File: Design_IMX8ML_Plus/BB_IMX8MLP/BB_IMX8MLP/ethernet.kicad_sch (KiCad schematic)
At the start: 40 parts, among them J5 RJ45_JK0654219, J6 RJ45_JK0654219, U1 KSZ9131RNXI, Y2 25MHz

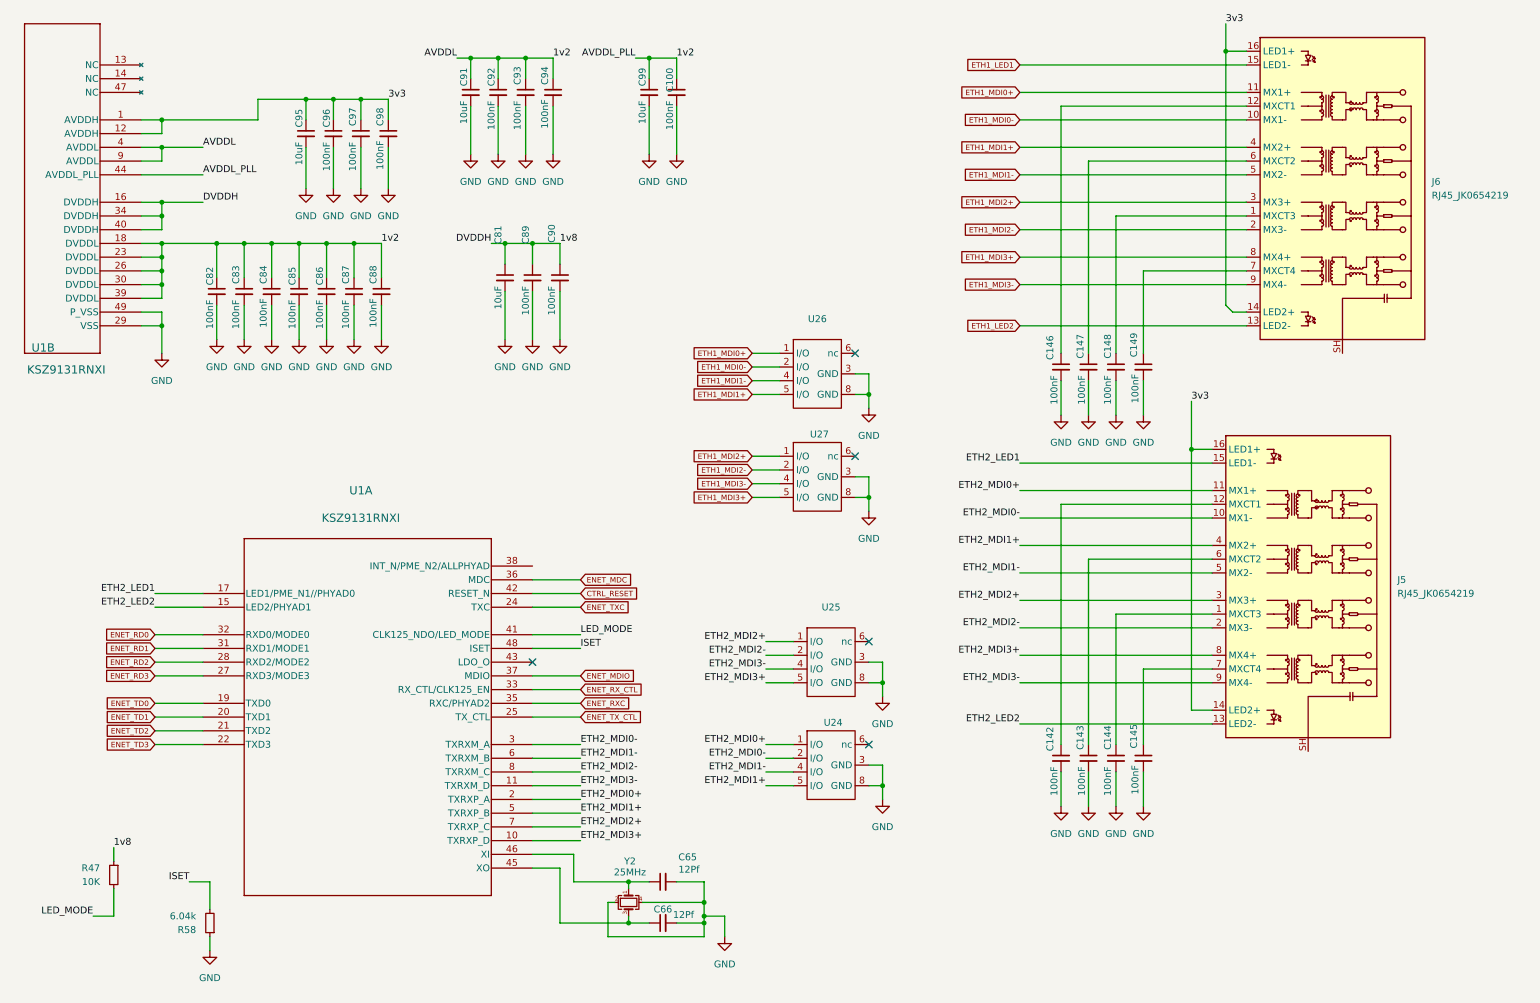
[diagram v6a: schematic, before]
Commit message: Board base resize
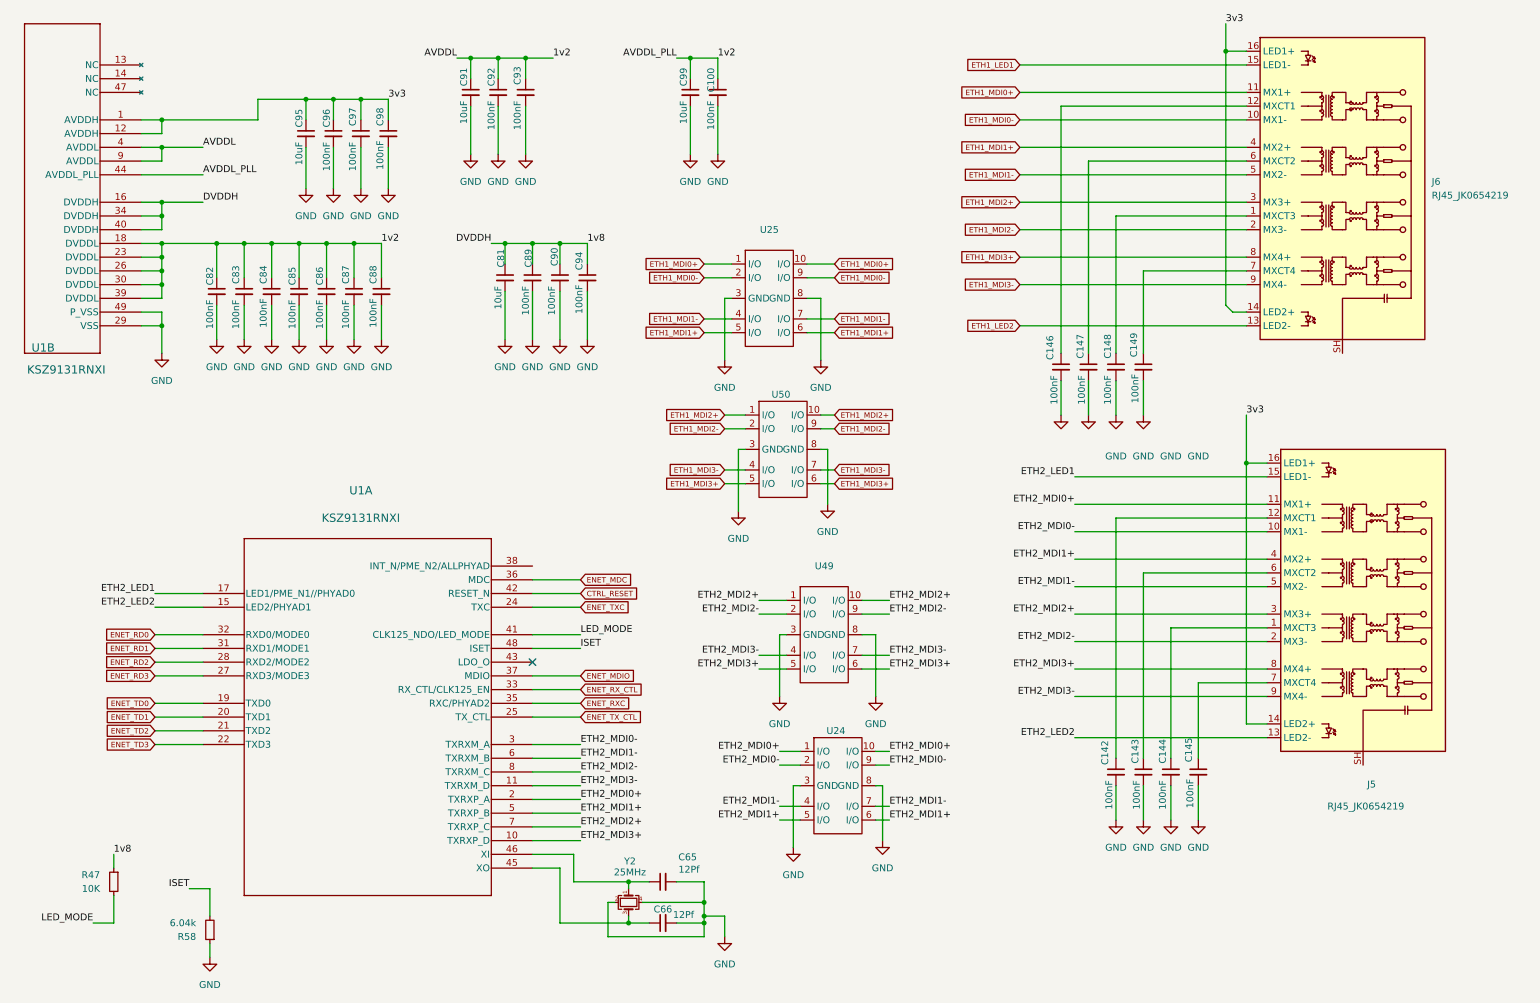
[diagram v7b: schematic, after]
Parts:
- removed U26, U27: ~, _W_SBC:DFN10_U-DFN2510-10_DIO, symbol _W_MX8M:D3V3F4U10LP-7
- added U49, U50: ~, _W_SBC:DFN10_U-DFN2510-10_DIO, symbol _W_MX8M:D3V3F4U10LP-7
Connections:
- net 1v2: no longer C94.1
- net 1v8: now also C94.1
- net ETH1_MDI0+: now also U25.1 (I/O), U25.10 (I/O)
- net ETH1_MDI0-: now also U25.2 (I/O), U25.9 (I/O)
- net ETH1_MDI1+: now also U25.5 (I/O), U25.6 (I/O)
- net ETH1_MDI1-: now also U25.4 (I/O), U25.7 (I/O)
- net ETH1_MDI2+: now also U50.1 (I/O), U50.10 (I/O)
- net ETH1_MDI2-: now also U50.2 (I/O), U50.9 (I/O)
- net ETH1_MDI3+: now also U50.5 (I/O), U50.6 (I/O)
- net ETH1_MDI3-: now also U50.4 (I/O), U50.7 (I/O)
- net ETH2_MDI0+: now also U24.10 (I/O)
- net ETH2_MDI0-: now also U24.9 (I/O)
- net ETH2_MDI1+: now also U24.6 (I/O)
- net ETH2_MDI1-: now also U24.7 (I/O)
- net ETH2_MDI2+: now also U49.1 (I/O), U49.10 (I/O); no longer U25.1 (I/O)
- net ETH2_MDI2-: now also U49.2 (I/O), U49.9 (I/O); no longer U25.2 (I/O)
- net ETH2_MDI3+: now also U49.5 (I/O), U49.6 (I/O); no longer U25.5 (I/O)
- net ETH2_MDI3-: now also U49.4 (I/O), U49.7 (I/O); no longer U25.4 (I/O)
- net GND: now also U49.3 (GND), U49.8 (GND), U50.3 (GND), U50.8 (GND)
- no-connect marks 5 -> 1
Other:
- moved on the sheet: C100, C142, C143, C144, C145, C94, C99, J5, R47, R58

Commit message: pcb reorganization
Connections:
- net ETH2_MDI1+: now also U24.4 (I/O), U24.7 (I/O); no longer U24.5 (I/O), U24.6 (I/O)
- net ETH2_MDI1-: now also U24.5 (I/O), U24.6 (I/O); no longer U24.4 (I/O), U24.7 (I/O)
- net ETH2_MDI3+: now also U49.4 (I/O), U49.7 (I/O); no longer U49.5 (I/O), U49.6 (I/O)
- net ETH2_MDI3-: now also U49.5 (I/O), U49.6 (I/O); no longer U49.4 (I/O), U49.7 (I/O)
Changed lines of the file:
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@@
 	)
 	(label "ETH2_MDI3+"
+		(at 175.26 132.08 0)
+		(effects
+			(font
+				(size 1.27 1.27)
+			)
+			(justify left bottom)
+		)
+	)
+	(label "ETH2_MDI3-"
 		(at 175.26 134.62 0)
-		(effects
-			(font
-				(size 1.27 1.27)
-			)
-			(justify left bottom)
-		)
-	)
-	(label "ETH2_MDI3-"
-		(at 175.26 132.08 0)
 		(effects
 			(font
@@
 	)
 	(label "ETH2_MDI1+"
-		(at 175.26 162.56 0)
+		(at 175.26 160.02 0)
 		(effects
 			(font
@@
 	)
 	(label "ETH2_MDI1-"
-		(at 154.94 160.02 180)
+		(at 154.94 162.56 180)
 		(effects
 			(font
@@
 	)
 	(label "ETH2_MDI1-"
-		(at 175.26 160.02 0)
+		(at 175.26 162.56 0)
 		(effects
 			(font
@@
 	)
 	(label "ETH2_MDI3+"
-		(at 151.13 134.62 180)
+		(at 151.13 132.08 180)
 		(effects
 			(font
@@
 	)
 	(label "ETH2_MDI1+"
-		(at 154.94 162.56 180)
+		(at 154.94 160.02 180)
 		(effects
 			(font
@@
 	)
 	(label "ETH2_MDI3-"
-		(at 151.13 132.08 180)
-		(effects
-			(font
+		(at 151.13 134.62 180)
+		(effects
+			(font
